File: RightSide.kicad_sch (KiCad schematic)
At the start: 28 parts, among them J3 USB_C_Receptacle_USB2.0_14P, J4 Conn_01x02, U2 AP2112K-3.3, U5 W25Q128JVS, U6 RP2040, Y2 12MHz Crystal GND24

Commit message: Added USBC interconnect
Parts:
- added J5: USB_C_Receptacle_USB2.0_14P, symbol Connector:USB_C_Receptacle_USB2.0_14P
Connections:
- net +3V3: now also J5.A4 (VBUS), J5.A9 (VBUS), J5.B4 (VBUS), J5.B9 (VBUS)
- net GND: now also J5.A1 (GND), J5.A12 (GND), J5.B1 (GND), J5.B12 (GND), J5.S1 (SHIELD)
- net GPIO_1: now reaches U6.3 (GPIO1)
- net GPIO_1: now also J5.A7 (D-), J5.B7 (D-)
- net GPIO_2: now reaches U6.4 (GPIO2)
- net GPIO_2: now also J5.A6 (D+), J5.B6 (D+)

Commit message: Added Footprints
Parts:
- removed J4: Conn_01x02, symbol Connector_Generic:Conn_01x02
- added SW28: SW_Push, symbol Switch:SW_Push
- added SW4: SW_Push, Button_Switch_SMD:Nidec_Copal_CAS-120A, symbol Switch:SW_Push
- C17, C18, C19, C20, C21, C22, C23, C24, C25, C26, C27, C28, C29, C30, C31, C32: footprint (none) -> Capacitor_SMD:C_0603_1608Metric_Pad1.08x0.95mm_HandSolder
- R10, R11, R12, R7, R8, R9: footprint (none) -> Resistor_SMD:R_0201_0603Metric_Pad0.64x0.40mm_HandSolder
- Y2: footprint (none) -> Crystal:Crystal_SMD_3225-4Pin_3.2x2.5mm
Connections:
- net +3.3V: no longer R12.2, U5.1 (~{CS})
- net GND: now also U6.19 (TESTEN), U6.57 (GND), SW28.1, SW4.1
- net RUN: now also SW4.2
- net QSPI_SD1: now reaches U5.2 (DO/IO_{1})
- net QSPI_SD1: now also U6.55 (QSPI_SD1)
- net QSPI_SD2: now reaches U5.3 (~{WP}/IO_{2})
- net QSPI_SD2: now also U6.54 (QSPI_SD2)
- net QSPI_SDO: now reaches U5.5 (DI/IO_{0})
- net QSPI_SDO: now also U6.53 (QSPI_SD0)
- net QSPI_SCLK: now reaches U5.6 (CLK)
- net QSPI_SCLK: now also U6.52 (QSPI_SCLK)
- net QSPI_SD3: now reaches U5.7 (~{HOLD}/~{RESET}/IO_{3})
- net QSPI_SD3: now also U6.51 (QSPI_SD3)
- net QSPI_SS: now reaches U6.56 (QSPI_SS)
- net QSPI_SS: now also R12.2, U5.1 (~{CS})
- net at R12.1: now also SW28.2

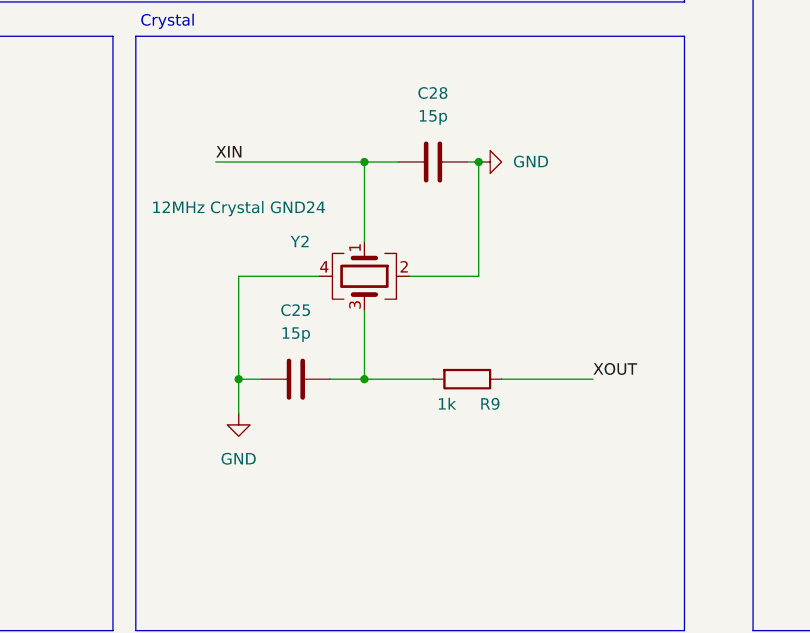
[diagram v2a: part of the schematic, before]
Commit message: Added footprints and started PCB layout
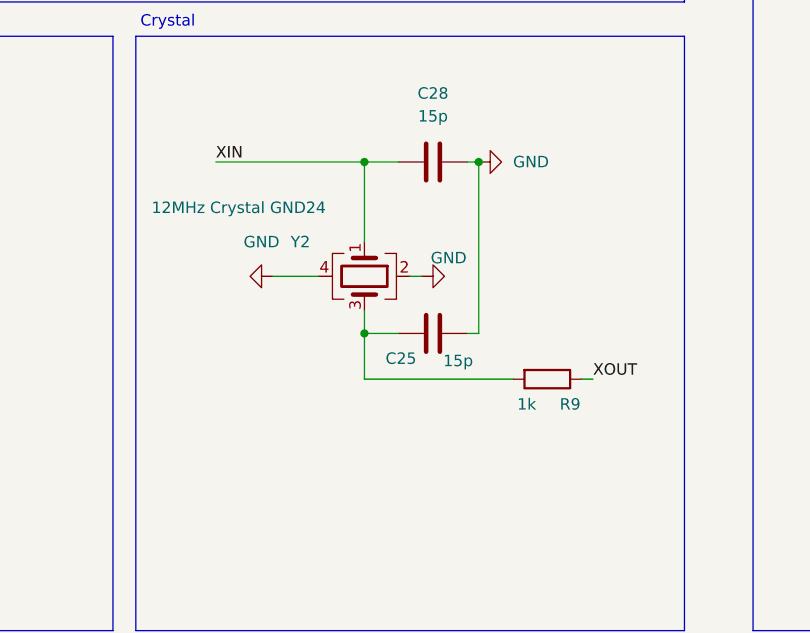
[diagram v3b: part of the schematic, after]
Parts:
- J3, J5: footprint (none) -> Connector_USB:USB_C_Receptacle_GCT_USB4125-xx-x-0190_6P_TopMnt_Horizontal
- SW28: footprint (none) -> PTS636_SM43J_SMTR_LFS:SW_PTS636_SM43J_SMTR_LFS
- SW4: footprint Button_Switch_SMD:Nidec_Copal_CAS-120A -> PTS636_SM43J_SMTR_LFS:SW_PTS636_SM43J_SMTR_LFS
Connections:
- net GND: now also C25.2; no longer C25.1
- net at R9.2, Y2.3: now also C25.1; no longer C25.2
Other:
- moved on the sheet: C25, R9
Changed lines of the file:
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@@
 	)
 	(junction
+		(at 229.87 217.17)
+		(diameter 0)
+		(color 0 0 0 0)
+	)
+	(junction
 		(at 241.3 35.56)
 		(diameter 0)
@@
 	)
 	(junction
-		(at 229.87 222.25)
-		(diameter 0)
-		(color 0 0 0 0)
-	)
-	(junction
-		(at 215.9 222.25)
-		(diameter 0)
-		(color 0 0 0 0)
-	)
-	(junction
 		(at 250.19 132.08)
 		(diameter 0)
@@
 	(wire
 		(pts
+			(xy 219.71 210.82) (xy 224.79 210.82)
+		)
+		(stroke
+			(width 0)
+			(type default)
+		)
+	)
+	(wire
+		(pts
 			(xy 161.29 49.53) (xy 151.13 49.53)
 		)
@@
 	(wire
 		(pts
+			(xy 241.3 217.17) (xy 242.57 217.17)
+		)
+		(stroke
+			(width 0)
+			(type default)
+		)
+	)
+	(wire
+		(pts
+			(xy 234.95 210.82) (xy 236.22 210.82)
+		)
+		(stroke
+			(width 0)
+			(type default)
+		)
+	)
+	(wire
+		(pts
 			(xy 330.2 55.88) (xy 330.2 62.23)
 		)
@@
 	(wire
 		(pts
-			(xy 229.87 222.25) (xy 237.49 222.25)
+			(xy 229.87 222.25) (xy 246.38 222.25)
 		)
 		(stroke
@@
 	(wire
 		(pts
-			(xy 191.77 130.81) (xy 193.04 130.81)
+			(xy 242.57 198.12) (xy 242.57 217.17)
 		)
 		(stroke
@@
 	(wire
 		(pts
-			(xy 229.87 222.25) (xy 226.06 222.25)
+			(xy 191.77 130.81) (xy 193.04 130.81)
 		)
 		(stroke
@@
 	(wire
 		(pts
-			(xy 215.9 222.25) (xy 215.9 226.06)
-		)
-		(stroke
-			(width 0)
-			(type default)
-		)
-	)
-	(wire
-		(pts
 			(xy 340.36 143.51) (xy 340.36 147.32)
 		)
@@
 	(wire
 		(pts
-			(xy 252.73 50.8) (xy 252.73 55.88)
+			(xy 229.87 217.17) (xy 233.68 217.17)
 		)
 		(stroke
@@
 	(wire
 		(pts
-			(xy 337.82 120.65) (xy 337.82 143.51)
+			(xy 252.73 50.8) (xy 252.73 55.88)
 		)
 		(stroke
@@
 	(wire
 		(pts
-			(xy 161.29 36.83) (xy 161.29 39.37)
+			(xy 337.82 120.65) (xy 337.82 143.51)
 		)
 		(stroke
@@
 	(wire
 		(pts
-			(xy 299.72 154.94) (xy 307.34 154.94)
+			(xy 161.29 36.83) (xy 161.29 39.37)
 		)
 		(stroke
@@
 	(wire
 		(pts
-			(xy 218.44 222.25) (xy 215.9 222.25)
+			(xy 299.72 154.94) (xy 307.34 154.94)
 		)
 		(stroke
@@
 	(wire
 		(pts
-			(xy 234.95 210.82) (xy 242.57 210.82)
-		)
-		(stroke
-			(width 0)
-			(type default)
-		)
-	)
-	(wire
-		(pts
 			(xy 161.29 80.01) (xy 161.29 82.55)
 		)
@@
 	(wire
 		(pts
-			(xy 242.57 210.82) (xy 242.57 198.12)
-		)
-		(stroke
-			(width 0)
-			(type default)
-		)
-	)
-	(wire
-		(pts
 			(xy 250.19 147.32) (xy 250.19 151.13)
 		)
@@
 	(wire
 		(pts
-			(xy 215.9 210.82) (xy 215.9 222.25)
-		)
-		(stroke
-			(width 0)
-			(type default)
-		)
-	)
-	(wire
-		(pts
 			(xy 241.3 50.8) (xy 241.3 46.99)
 		)
@@
 	(wire
 		(pts
-			(xy 229.87 214.63) (xy 229.87 222.25)
+			(xy 229.87 214.63) (xy 229.87 217.17)
 		)
 		(stroke
@@
 	(wire
 		(pts
-			(xy 245.11 222.25) (xy 255.27 222.25)
+			(xy 254 222.25) (xy 255.27 222.25)
 		)
 		(stroke
@@
 	(wire
 		(pts
+			(xy 229.87 217.17) (xy 229.87 222.25)
+		)
+		(stroke
+			(width 0)
+			(type default)
+		)
+	)
+	(wire
+		(pts
 			(xy 327.66 120.65) (xy 327.66 143.51)
 		)
@@
 	(wire
 		(pts
-			(xy 224.79 210.82) (xy 215.9 210.82)
-		)
-		(stroke
-			(width 0)
-			(type default)
-		)
-	)
-	(wire
-		(pts
 			(xy 358.14 160.02) (xy 365.76 160.02)
 		)
@@
 			)
 		)
-		(property "Footprint" "Button_Switch_SMD:Nidec_Copal_CAS-120A"
+		(property "Footprint" "PTS636_SM43J_SMTR_LFS:SW_PTS636_SM43J_SMTR_LFS"
 			(at 110.49 26.67 0)
 			(hide yes)
@@
 	(symbol
 		(lib_id "Device:C")
-		(at 222.25 222.25 90)
+		(at 237.49 217.17 90)
 		(unit 1)
 		(body_style 1)
@@
 		(in_pos_files yes)
 		(dnp no)
-		(fields_autoplaced yes)
 		(property "Reference" "C25"
-			(at 222.25 214.63 90)
+			(at 233.934 219.964 90)
 			(show_name no)
 			(do_not_autoplace no)
@@
 		)
 		(property "Value" "15p"
-			(at 222.25 217.17 90)
+			(at 240.284 220.218 90)
 			(show_name no)
 			(do_not_autoplace no)
@@
 		)
 		(property "Footprint" "Capacitor_SMD:C_0603_1608Metric_Pad1.08x0.95mm_HandSolder"
-			(at 226.06 221.2848 0)
+			(at 241.3 216.2048 0)
 			(hide yes)
 			(show_name no)
@@
 		)
 		(property "Datasheet" ""
-			(at 222.25 222.25 0)
+			(at 237.49 217.17 0)
 			(hide yes)
 			(show_name no)
@@
 		)
 		(property "Description" "Unpolarized capacitor"
-			(at 222.25 222.25 0)
+			(at 237.49 217.17 0)
 			(hide yes)
 			(show_name no)
@@
 	(symbol
 		(lib_id "Device:R")
-		(at 241.3 222.25 270)
+		(at 250.19 222.25 270)
 		(unit 1)
 		(body_style 1)
@@
 		(dnp no)
 		(property "Reference" "R9"
-			(at 243.84 225.044 90)
+			(at 252.73 225.044 90)
 			(show_name no)
 			(do_not_autoplace no)
@@
 		)
 		(property "Value" "1k"
-			(at 239.014 225.044 90)
+			(at 247.904 225.044 90)
 			(show_name no)
 			(do_not_autoplace no)
@@
 		)
 		(property "Footprint" "Resistor_SMD:R_0201_0603Metric_Pad0.64x0.40mm_HandSolder"
-			(at 241.3 220.472 90)
+			(at 250.19 220.472 90)
 			(hide yes)
 			(show_name no)
@@
 		)
 		(property "Datasheet" ""
-			(at 241.3 222.25 0)
+			(at 250.19 222.25 0)
 			(hide yes)
 			(show_name no)
@@
 		)
 		(property "Description" "Resistor"
-			(at 241.3 222.25 0)
+			(at 250.19 222.25 0)
 			(hide yes)
 			(show_name no)
@@
 			)
 		)
-		(property "Footprint" ""
+		(property "Footprint" "Connector_USB:USB_C_Receptacle_GCT_USB4125-xx-x-0190_6P_TopMnt_Horizontal"
 			(at 172.72 142.24 0)
 			(hide yes)
@@
 			)
 		)
-		(property "Footprint" ""
+		(property "Footprint" "Connector_USB:USB_C_Receptacle_GCT_USB4125-xx-x-0190_6P_TopMnt_Horizontal"
 			(at 162.56 213.36 0)
 			(hide yes)
@@
 	(symbol
 		(lib_id "power:GND")
-		(at 215.9 226.06 0)
+		(at 219.71 210.82 270)
 		(unit 1)
 		(body_style 1)
@@
 		(fields_autoplaced yes)
 		(property "Reference" "#PWR033"
-			(at 215.9 232.41 0)
+			(at 213.36 210.82 0)
 			(hide yes)
 			(show_name no)
@@
 		)
 		(property "Value" "GND"
-			(at 215.9 231.14 0)
+			(at 218.44 207.01 90)
 			(show_name no)
 			(do_not_autoplace no)
@@
 		)
 		(property "Footprint" ""
-			(at 215.9 226.06 0)
+			(at 219.71 210.82 0)
 			(hide yes)
 			(show_name no)
@@
 		)
 		(property "Datasheet" ""
-			(at 215.9 226.06 0)
+			(at 219.71 210.82 0)
 			(hide yes)
 			(show_name no)
@@
 		)
 		(property "Description" "Power symbol creates a global label with name \"GND\" , ground"
-			(at 215.9 226.06 0)
+			(at 219.71 210.82 0)
 			(hide yes)
 			(show_name no)
@@
 			)
 		)
-		(property "Footprint" ""
+		(property "Footprint" "PTS636_SM43J_SMTR_LFS:SW_PTS636_SM43J_SMTR_LFS"
 			(at 288.29 62.23 0)
 			(hide yes)
@@
 					(unit 1)
 				)
+			)
+		)
+	)
+	(symbol
+		(lib_id "power:GND")
+		(at 236.22 210.82 90)
+		(unit 1)
+		(body_style 1)
+		(exclude_from_sim no)
+		(in_bom yes)
+		(on_board yes)
+		(in_pos_files yes)
+		(dnp no)
+		(property "Reference" "#PWR09"
+			(at 242.57 210.82 0)
+			(hide yes)
+			(show_name no)
+			(do_not_autoplace no)
+			(effects
+				(font
+					(size 1.27 1.27)
+				)
+			)
+		)
+		(property "Value" "GND"
+			(at 237.236 208.788 90)
+			(show_name no)
+			(do_not_autoplace no)
+			(effects
+				(font
+					(size 1.27 1.27)
+				)
+				(justify right)
+			)
+		)
+		(property "Footprint" ""
+			(at 236.22 210.82 0)
+			(hide yes)
+			(show_name no)
+			(do_not_autoplace no)
+			(effects
+				(font
+					(size 1.27 1.27)
+				)
+			)
+		)
+		(property "Datasheet" ""
+			(at 236.22 210.82 0)
+			(hide yes)
+			(show_name no)
+			(do_not_autoplace no)
+			(effects
+				(font
+					(size 1.27 1.27)
+				)
+			)
+		)
+		(property "Description" "Power symbol creates a global label with name \"GND\" , ground"
+			(at 236.22 210.82 0)
+			(hide yes)
+			(show_name no)
+			(do_not_autoplace no)
+			(effects
+				(font
+					(size 1.27 1.27)
+				)
+			)
+		)
+		(pin "1"
+		)
+		(instances
+			(project "Keybrd_Part_2"
+				(path "/81b42d2b-3549-47f3-9495-e592cbed5536/e54e4537-1233-4890-adb4-9db6da850684"
+					(reference "#PWR09")
+					(unit 1)
+				)
